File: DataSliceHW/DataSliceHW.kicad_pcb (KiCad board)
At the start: 2 copper layers, 85.5 x 54 mm, 185 parts, among them J1 USB4105-GF-A, J2 DM3D-SF, J3 53261-0271, J4 68712414522, J5 66011102111302, J6 USB4105-GF-A, Q1 BC847BDW1, SW1 K3-1391D-5MM, U1 ESP32-S3-WROOM-1, U2 CP2102N-A02-GQFN28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

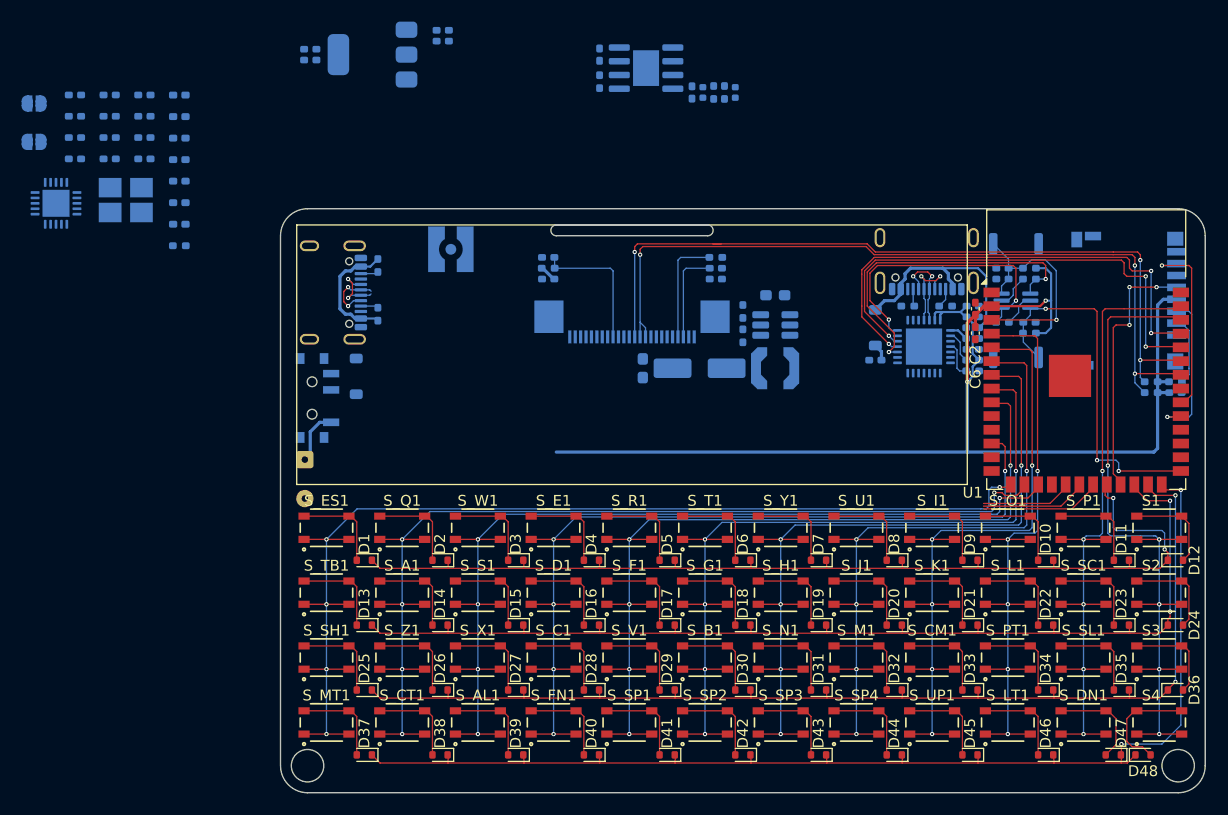
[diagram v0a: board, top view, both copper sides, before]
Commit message: Finalized firt prototype Completed PCB design Finalized schematic
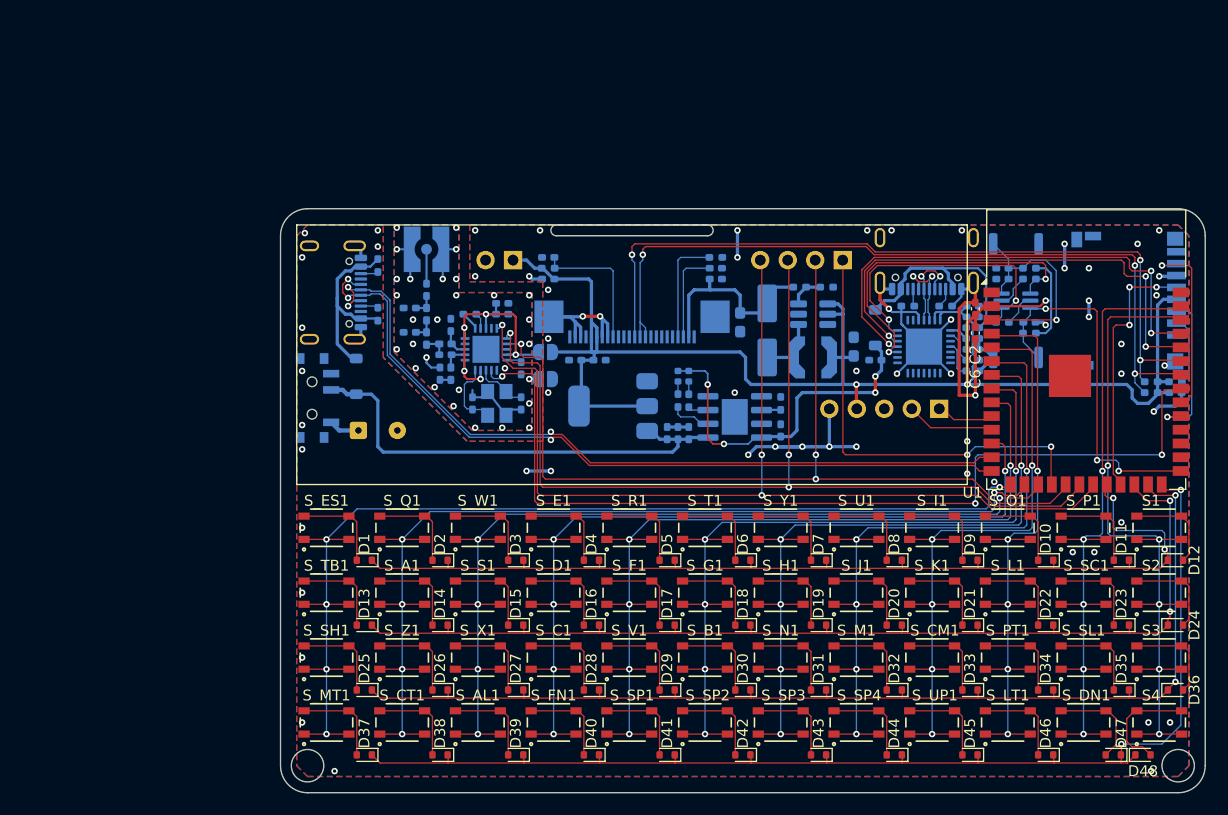
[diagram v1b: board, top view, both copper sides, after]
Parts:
- removed the C26 at (44.5, 26.7)
- removed the C30 at (41.2, 24.7)
- removed C34: 12pF(5%)NP0, Capacitor_SMD:C_0402_1005Metric_Pad0.74x0.62mm_HandSolder
- removed L6: 3.3nH(5%), Inductor_SMD:L_0402_1005Metric_Pad0.77x0.64mm_HandSolder
- removed L7: 12nH(5%), Inductor_SMD:L_0402_1005Metric_Pad0.77x0.64mm_HandSolder
- removed L8: 18nH(5%), Inductor_SMD:L_0402_1005Metric_Pad0.77x0.64mm_HandSolder
- added C27: 220pF(5%)NP0, Capacitor_SMD:C_0402_1005Metric_Pad0.74x0.62mm_HandSolder, B.Cu at (73.8, 42.8)
- added C32: 12pF(5%)NP0, Capacitor_SMD:C_0402_1005Metric_Pad0.74x0.62mm_HandSolder, B.Cu at (78.0, 53.2)
- added G***: LOGO, LOGO, B.Cu at (85.8, 71.5)
- added J4: Conn_01x04, Connector_PinHeader_2.54mm:PinHeader_1x04_P2.54mm_Horizontal, B.Cu at (112.2, 40.0)
- added J5: Conn_01x02, Connector_PinHeader_2.54mm:PinHeader_1x02_P2.54mm_Horizontal, B.Cu at (81.8, 40.0)
- added J9: Conn_01x05, Connector_PinSocket_2.54mm:PinSocket_1x05_P2.54mm_Vertical, B.Cu at (121.2, 53.8)
- C23: value 100pF(5%)NP0 -> 0.1uF(10%)X5R
- C24: value 0.1uF(10%)X5R -> 220pF(5%)NP0
- C25, C31: value 12pF(5%)NP0 -> 3.9pF(5%)NP0
- C28: value 1pF(5%)NP0 -> 8.2pF(5%)NP0
- C29: value 47pF(5%)NP0 -> 5.6pF(5%)NP0
- C33: value 1.5pF(5%)NP0 -> 12pF(5%)NP0
- L2: value 18nH(5%) -> 27nH(5%)
- L3: value 12nH(5%) -> 22nH(5%)
- L4, L5: value 12nH(5%) -> 27nH(5%)
- Y1: footprint Crystal:Crystal_SMD_3225-4Pin_3.2x2.5mm_HandSoldering -> Crystal:Crystal_SMD_3225-4Pin_3.2x2.5mm
- moved R23 52.6 mm to (84.8, 48.5), turned to 0 degrees
- moved R24 52.1 mm to (84.8, 51.0), turned to 0 degrees
- moved C33 48.0 mm to (82.5, 53.2), turned to -90 degrees
- moved C11 43.1 mm to (97.0, 56.0), turned to 90 degrees
- moved U6 42.0 mm to (79.2, 48.2)
- moved C10 41.8 mm to (96.0, 56.0), turned to -90 degrees
- moved C23 40.8 mm to (82.5, 50.0), turned to -90 degrees
- moved C31 39.8 mm to (76.0, 46.0), turned to 90 degrees
- moved U3 39.4 mm to (91.0, 53.5)
- moved C25 39.3 mm to (75.5, 48.8)
- moved Y1 39.1 mm to (80.2, 53.2), turned to 90 degrees
- moved C12 38.5 mm to (89.8, 49.2), turned to 0 degrees
- moved C18 38.3 mm to (80.8, 44.0)
- moved C20 37.8 mm to (80.8, 45.0), turned to 0 degrees
- moved C13 37.8 mm to (87.5, 49.2)
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- renumbered C27 to C26, C32 to C30, J4 to J6, J6 to J7, J5 to J8
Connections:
- C23 pad 1: Net-(C23-Pad1) -> Net-(U6-DCOUPL)
- C24 pad 1: Net-(U6-DCOUPL) -> Net-(C24-Pad1)
- C25 pad 1: Net-(C25-Pad1) -> Net-(U6-RF_P)
- C25 pad 2: Net-(J5-In) -> Net-(C25-Pad2)
- C28 pad 1: Net-(C26-Pad1) -> Net-(C28-Pad1)
- C28 pad 2: Net-(C28-Pad2) -> GNDA
- C29 pad 1: Net-(C25-Pad1) -> GNDA
- C29 pad 2: Net-(C29-Pad2) -> Net-(C27-Pad1)
- C31 pad 1: Net-(U6-XOSC_Q1) -> Net-(U6-RF_N)
- C33 pad 1: Net-(C28-Pad2) -> Net-(U6-XOSC_Q1)
- J6 pad Z1: unconnected-(J4-PadZ1) -> GND
- J6 pad Z2: unconnected-(J4-PadZ2) -> GND
- J8 pad 1: Net-(J5-In) -> Net-(J8-In)
- L2 pad 1: Net-(C26-Pad1) -> Net-(U6-RF_P)
- L2 pad 2: Net-(C23-Pad1) -> Net-(C24-Pad1)
- L3 pad 1: Net-(U6-RF_P) -> Net-(C25-Pad2)
- L3 pad 2: Net-(C26-Pad1) -> Net-(C28-Pad1)
- L4 pad 1: Net-(C26-Pad2) (its old number) -> Net-(C28-Pad1)
- L4 pad 2: Net-(C30-Pad1) -> Net-(C27-Pad1)
- L5 pad 1: Net-(C30-Pad1) -> Net-(C25-Pad2)
- L5 pad 2: Net-(C25-Pad1) -> Net-(U6-RF_N)
- Y1 pad 2: unconnected-(Y1-Pad2) -> GNDA
- Y1 pad 4: unconnected-(Y1-Pad4) -> GNDA
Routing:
- net GND: track 0.00 -> 107.4 mm, vias 0 -> 64
- net /SUB_CS: track 0.00 -> 86.5 mm, vias 0 -> 3
- net /SPI_DO: track 11.2 -> 93.6 mm, vias 0 -> 3
- net /SPI_CK: track 9.87 -> 89.9 mm, vias 0 -> 3
- net /SPI_DI: track 8.50 -> 85.8 mm, vias 0 -> 3
- net /HOST_DP: track 5.79 -> 73.2 mm, vias 2 -> 3
- net /HOST_DN: track 5.79 -> 73.2 mm, vias 2 -> 3
- net +BATT: track 0.00 -> 43.8 mm
- net /SPI_CS: track 0.00 -> 41.0 mm, vias 0 -> 2
- net VCC: track 116.9 -> 152.8 mm, vias 2 -> 3
- net +5V: track 1.59 -> 34.2 mm, vias 0 -> 4
- net VDDA: track 0.00 -> 25.7 mm, vias 0 -> 5
- net GNDA: track 0.00 -> 19.1 mm, vias 0 -> 29
- net VPP: track 0.00 -> 18.3 mm
- net /RS_RX: track 0.00 -> 8.76 mm
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- added copper zone on B.Cu, net GND
- added copper zone on F.Cu, net GND
- added copper zone on B.Cu, net GNDA
- added copper zone on F.Cu, net GNDA

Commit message: Minor silkscreen update
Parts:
- moved G*** 0.35 mm to (85.5, 71.8)

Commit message: Minor PCB changes
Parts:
- removed the R23 at (84.8, 48.5)
- removed R24: 0R, Jumper:SolderJumper-2_P1.3mm_Open_RoundedPad1.0x1.5mm
- renumbered R25 to R23
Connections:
- C18 pad 1: GNDA -> GND
- C18 pad 2: VDDA -> VCC
- C20 pad 1: VDDA -> VCC
- C20 pad 2: GNDA -> GND
- C23 pad 2: GNDA -> GND
- C24 pad 2: GNDA -> GND
- C28 pad 2: GNDA -> GND
- C29 pad 1: GNDA -> GND
- C31 pad 2: GNDA -> GND
- C32 pad 1: GNDA -> GND
- C33 pad 2: GNDA -> GND
- J8 pad 2: GNDA -> GND
- R23 pad 2: GNDA -> GND
- U6 pad 11: VDDA -> VCC
- U6 pad 14: VDDA -> VCC
- U6 pad 15: VDDA -> VCC
- U6 pad 16: GNDA -> GND
- U6 pad 18: VDDA -> VCC
- U6 pad 19: GNDA -> GND
- U6 pad 21: GNDA -> GND
- U6 pad 4: VDDA -> VCC
- U6 pad 9: VDDA -> VCC
- Y1 pad 2: GNDA -> GND
- Y1 pad 4: GNDA -> GND
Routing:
- net VCC: track 152.8 -> 179.5 mm, vias 3 -> 8
- net VDDA: track 25.7 -> 0.00 mm, vias 5 -> 0
- net GNDA: track 19.1 -> 0.00 mm, vias 29 -> 0
- net GND: track 107.4 -> 118.7 mm, vias 64 -> 102
- net /KB_C_2: track 89.4 -> 95.3 mm
- net /KB_C_1: track 95.5 -> 101.4 mm
- net /KB_C_0: track 100.8 -> 106.7 mm
- net /SPI_DO: track 93.6 -> 91.7 mm
- net /SPI_CK: track 89.9 -> 88.4 mm
- net /SUB_CS: track 86.5 -> 85.5 mm
- net /SPI_DI: track 85.8 -> 85.2 mm
- removed copper zone on B.Cu, net GNDA
- removed copper zone on F.Cu, net GNDA
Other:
- outline, holes or cut-outs redrawn
